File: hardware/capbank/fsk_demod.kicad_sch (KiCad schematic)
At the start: 14 parts, among them U10 TS861IL, U7 4046

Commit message: Small hardware changes
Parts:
- U7: value 4046 -> 74HC4046AD; footprint Package_DIP:DIP-16_W7.62mm -> Package_SO:SOIC-16_3.9x9.9mm_P1.27mm
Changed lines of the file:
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@@
 			)
 		)
-		(property "Value" "4046"
+		(property "Value" "74HC4046AD"
 			(at 69.4533 105.41 0)
 			(effects
@@
 			)
 		)
-		(property "Footprint" "Package_DIP:DIP-16_W7.62mm"
+		(property "Footprint" "Package_SO:SOIC-16_3.9x9.9mm_P1.27mm"
 			(at 67.31 120.65 0)
 			(effects

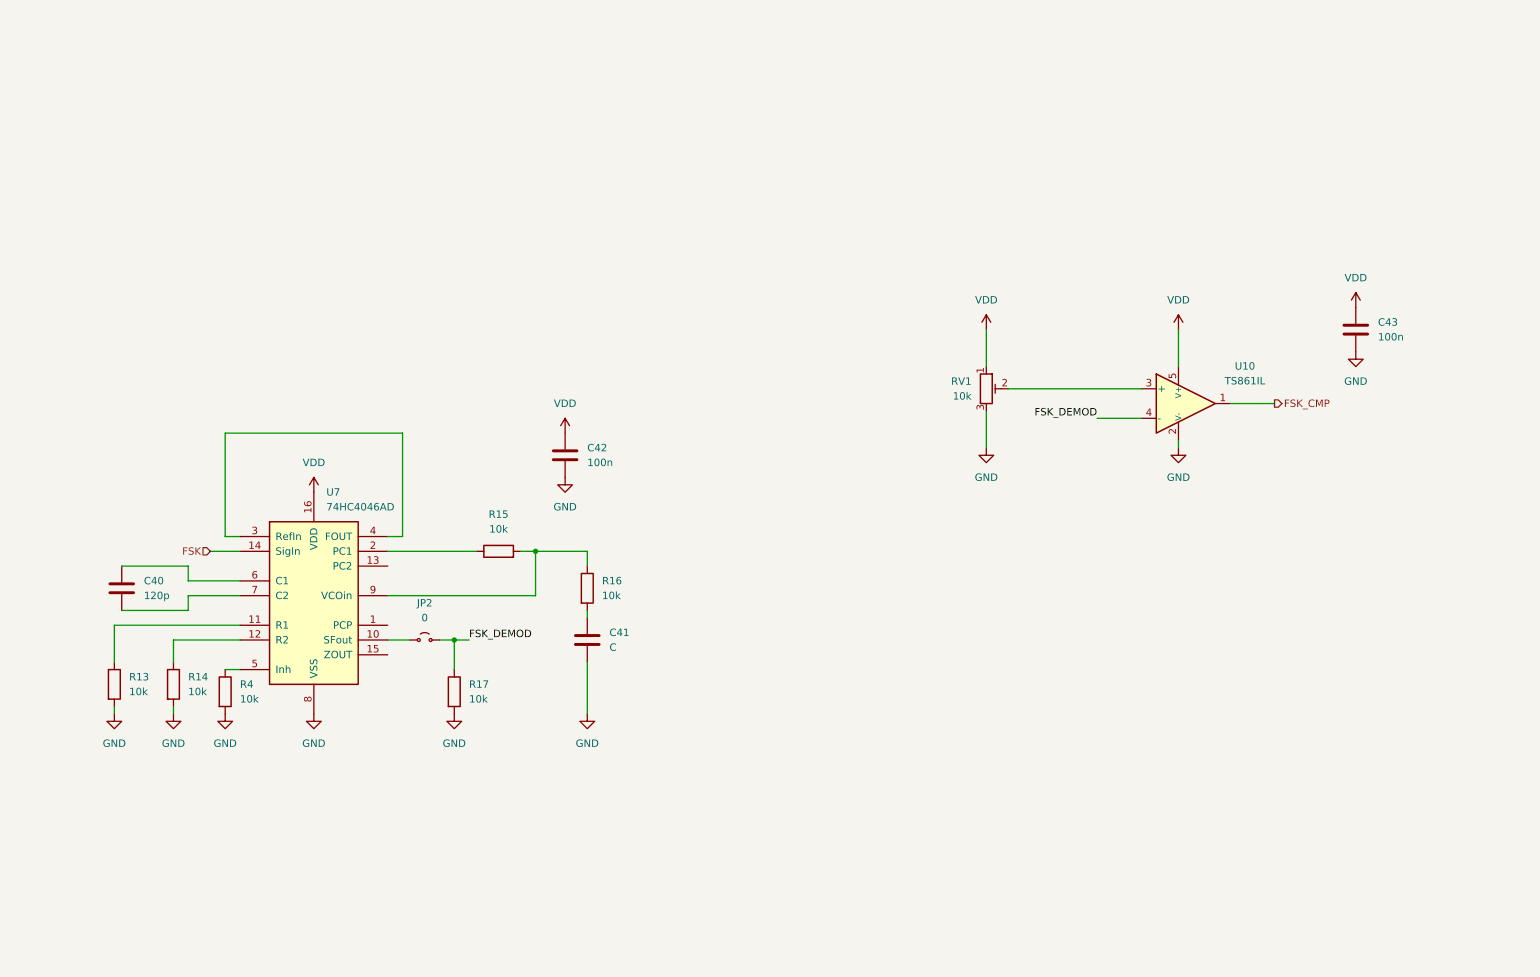
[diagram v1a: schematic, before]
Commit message: Add footprint for buffered-filter and replace pot with digital pot
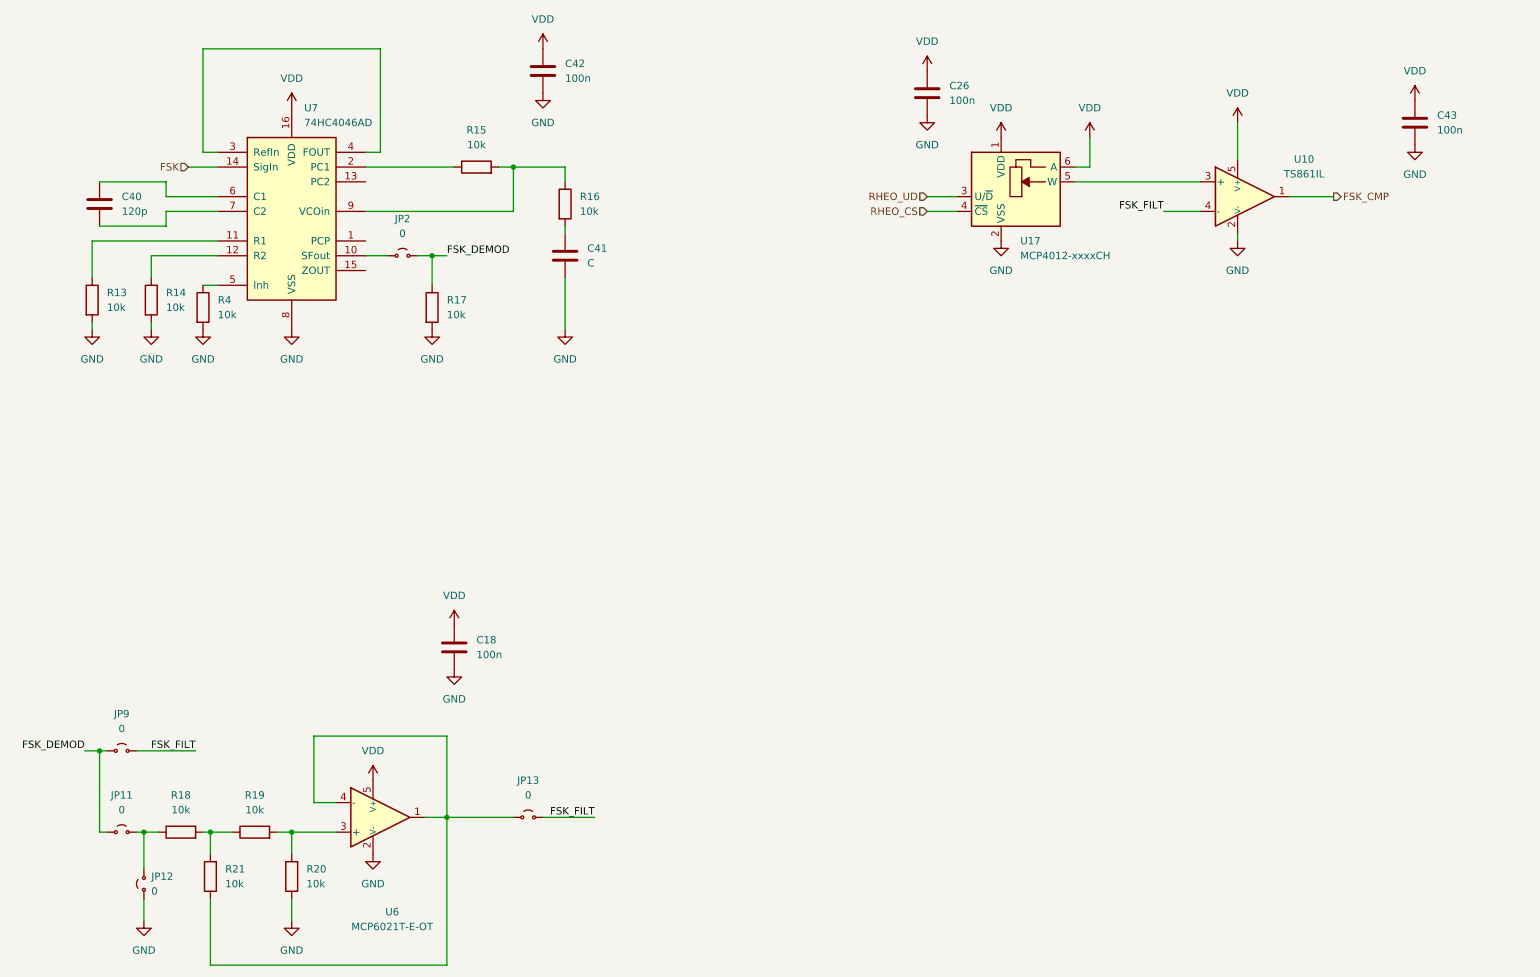
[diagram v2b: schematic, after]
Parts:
- removed RV1: 10k, PCM_Potentiometer_THT_AKL:Potentiometer_Piher_PT-10-V10_Vertical, symbol Device:R_Potentiometer_Trim
- added C18, C26: 100n, PCM_Capacitor_SMD_AKL:C_0603_1608Metric, symbol Device:C
- added JP11, JP12, JP13, JP9: 0, PCM_Resistor_SMD_AKL:R_0603_1608Metric, symbol Jumper:Jumper_2_Small_Open
- added R18, R19, R20, R21: 10k, PCM_Resistor_SMD_AKL:R_0603_1608Metric, symbol Device:R
- added U17: MCP4012-xxxxCH, Package_TO_SOT_SMD:SOT-23-6, symbol Potentiometer_Digital:MCP4012-xxxxCH
- added U6: MCP6021T-E-OT, PCM_Package_TO_SOT_SMD_AKL:SOT-23-5, symbol PCM_Amplifier_Operational_AKL:MCP6021T-E-OT
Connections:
- net FSK_DEMOD: now also JP11.1 (A), JP9.1 (A); no longer U10.4 (-)
- net GND: now also C18.2, C26.2, JP12.1 (A), R20.1, U17.2 (VSS), U6.2 (V-)
- net VDD: now also C18.1, C26.1, U17.1 (VDD), U17.6 (A), U6.5 (V+)
- net at U10.3 (+): now also U17.5 (W)
- new net: JP11.2 (B), JP12.2 (B), R18.1
- new net: R18.2, R19.1, R21.2
- new net: R19.2, R20.2, U6.3 (+)
- new net: JP13.1 (A), R21.1, U6.1, U6.4 (-)
- new net FSK_FILT: JP13.2 (B), JP9.2 (B), U10.4 (-)
- new net RHEO_CS: U17.4 (~{CS})
- new net RHEO_UD: U17.3 (U/~{D})
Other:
- moved on the sheet: C40, C41, C42, C43, JP2, R13, R14, R15, R16, R17, R4, U10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

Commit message: Update PCB with learned lessons
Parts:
- added C34: 100n, PCM_Capacitor_SMD_AKL:C_0603_1608Metric, symbol Device:C
- added JP14, JP15, JP16: 0, PCM_Resistor_SMD_AKL:R_0603_1608Metric, symbol Jumper:Jumper_2_Small_Open
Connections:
- net GND: now also C34.2
- net VCO_IN: now reaches R15.2, R16.1, U7.9 (VCOin)
- net VCO_IN: now also C34.1
- net at U7.2 (PC1): now also JP16.1 (A); no longer R15.1
- net at U7.13 (PC2): now also JP15.1 (A)
- net at U7.15 (ZOUT): now also JP14.1 (A)
- new net PC: JP14.2 (B), JP15.2 (B), JP16.2 (B), R15.1
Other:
- moved on the sheet: C26, C41, C43, JP2, R15, R16, R17, U10, U17

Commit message: Add hysteresis to comparator
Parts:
- removed R20, R21: 10k, PCM_Resistor_SMD_AKL:R_0603_1608Metric, symbol Device:R
- removed U17: MCP4012-xxxxCH, Package_TO_SOT_SMD:SOT-23-6, symbol Potentiometer_Digital:MCP4012-xxxxCH
- added C14, C36: 1n, PCM_Capacitor_SMD_AKL:C_0603_1608Metric, symbol Device:C
- added R25: 10k, PCM_Resistor_SMD_AKL:R_0603_1608Metric, symbol Device:R
- added R26: 200k, PCM_Resistor_SMD_AKL:R_0603_1608Metric, symbol Device:R
- added U18: MCP4013-xxxxCH, Package_TO_SOT_SMD:SOT-23-6, symbol Potentiometer_Digital:MCP4013-xxxxCH
- C34: value 100n -> 1n
- C41: value C -> 100n
- R15: value 10k -> 285k
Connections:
- net FSK_CMP: now also R26.1
- net GND: now also C14.2, U18.2 (VSS)
- net RHEO_CS: now also U18.4 (~{CS})
- net RHEO_UD: now also U18.3 (U/~{D})
- net VDD: now also U18.1 (VDD), U18.6 (A)
- net at U10.3 (+): now also R25.2, R26.2
- net at R18.2, R19.1: now also C36.1
- net at R19.2, U6.3 (+): now also C14.1
- net at JP13.1 (A), U6.1, U6.4 (-): now also C36.2
- new net: R25.1, U18.5 (W)
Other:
- note added: "For 74HC_HCT4046A (dataset names): fl = 100kHz R1C1 = 4e-5 (40us) foff = 90kHz R2 = 150kOhm C1 = 700pF R1 = 57kOhm (R2C1 = 105us)"
- note added: "For cd74hc4046a (dataset names): f0 = 250kHz fl = 100kHz fmin = 90kHz fmax = 410kHz VCC = 5V R2 = 22k C1 = 2~3nF R2/R1 = ~3 R1 = 7.4k (maybe a bit lower) (R1C1 = 18.5us) (R2C1 = 55us)"
- note added: "I[output positive] = (VCC - x * VCC) / (R26 + R_series) I[output negative] = x * VCC / (R26 + R_series)"
- note added: "Thevenin equivalent R_series = x (1-x) * 10k + R25 V = x * VCC"
- note added: "Up to first order, for R26 >> R25 and R_[MCP] ~= R25: V+[output positive] = VCC * x + VCC * R25 / R26 V+[output negative] = VCC * x - VCC * R25 / R26 V+[output positive] > V+[output_negative] (If FSK_FILT < V+, output is positive, once FSK_FILT crosses V+, output jumps to negative, and as expected the V+ jumps a bit downwards)"
- moved on the sheet: C34, C41, R15, R16

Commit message: Various wiring fixes and add bleed resistor to antenna
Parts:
- C36: value 1n -> 2n
- R18, R19: value 10k -> 1.7k
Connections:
- no-connect marks 0 -> 1
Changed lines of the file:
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@@
 		(color 0 0 0 0)
 	)
+	(no_connect
+		(at 76.2 59.69)
+	)
 	(wire
 		(pts
@@
 			)
 		)
-		(property "Value" "10k"
+		(property "Value" "1.7k"
 			(at 44.45 157.48 90)
 			(effects
@@
 			)
 		)
-		(property "Value" "10k"
+		(property "Value" "1.7k"
 			(at 57.15 157.48 90)
 			(effects
@@
 			)
 		)
-		(property "Value" "1n"
+		(property "Value" "2n"
 			(at 53.34 170.1799 0)
 			(effects

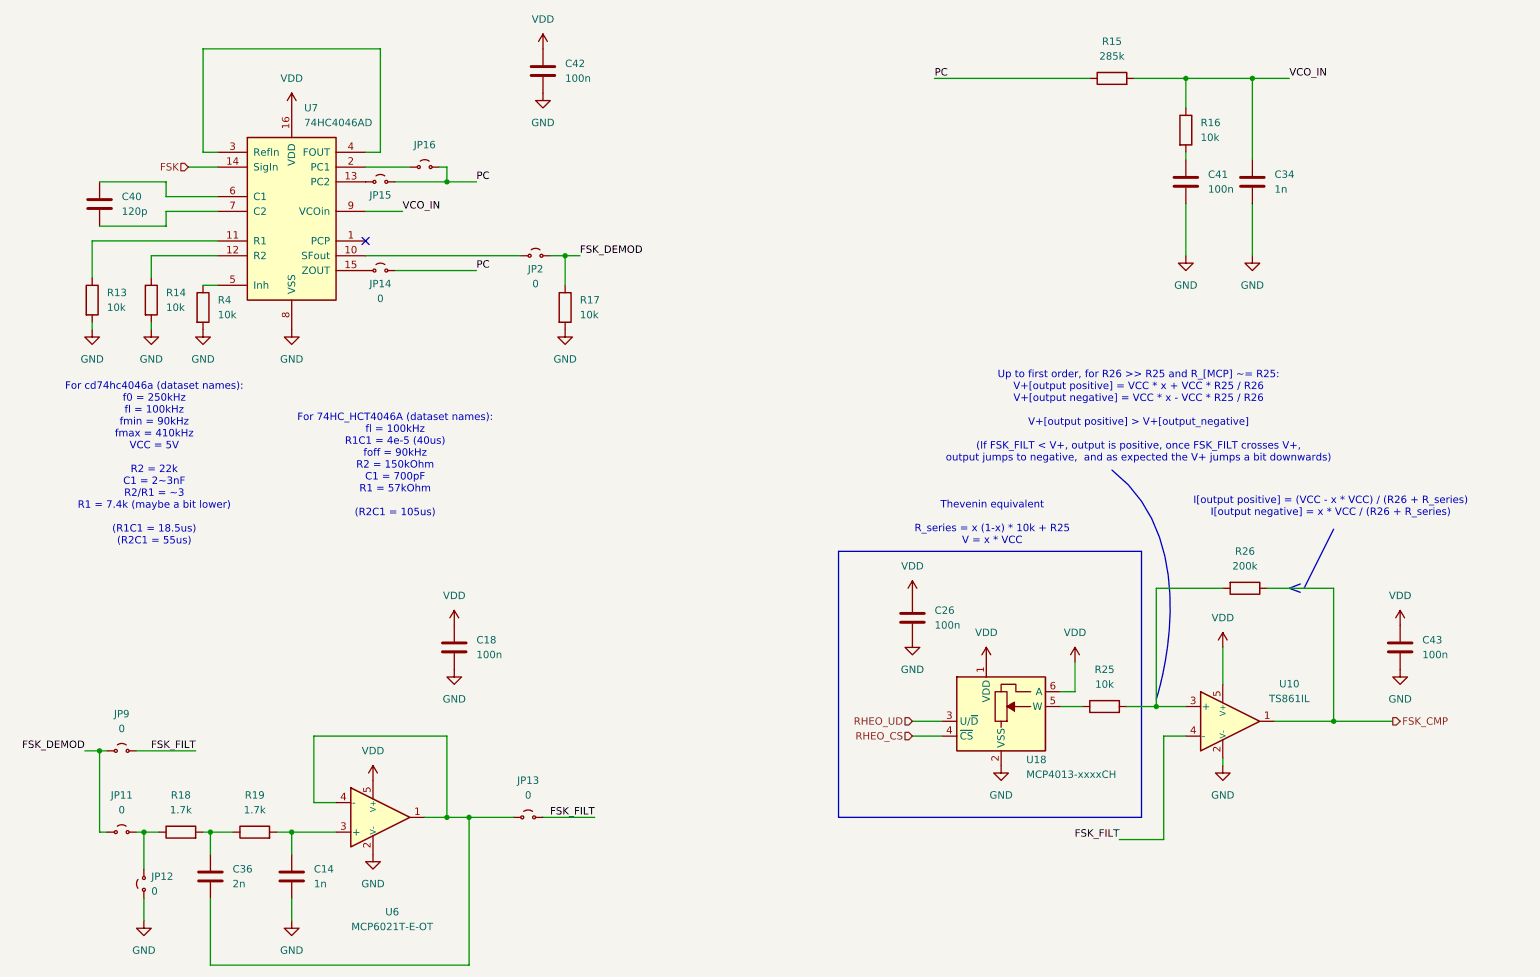
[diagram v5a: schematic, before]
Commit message: Update values after breadboard testing
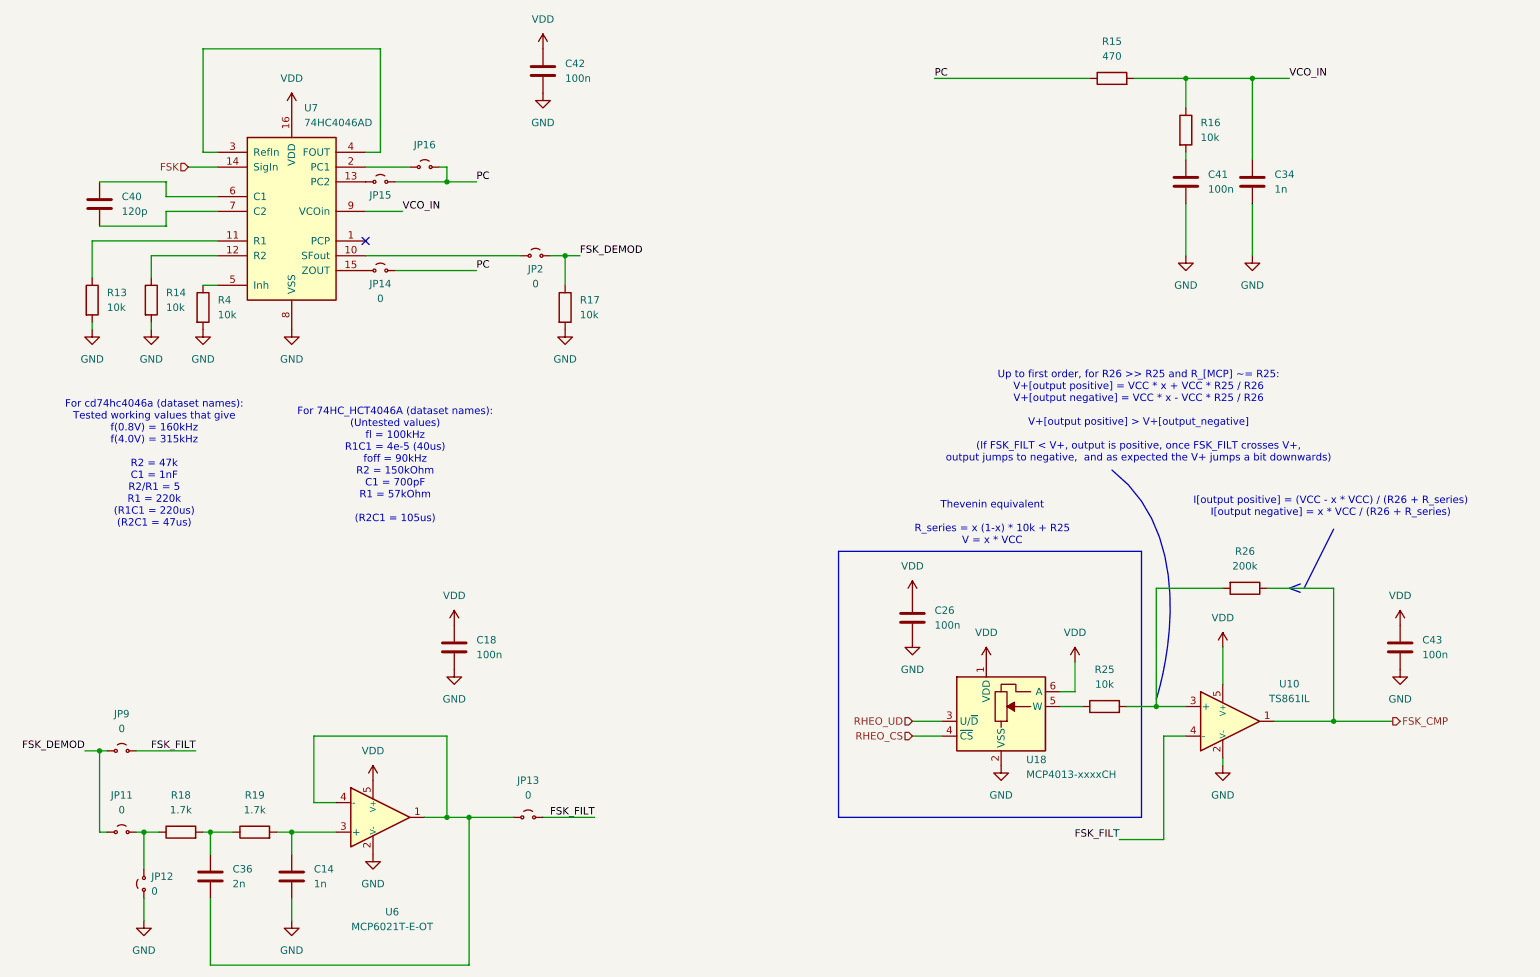
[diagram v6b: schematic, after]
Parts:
- R15: value 285k -> 470
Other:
- note added: "For 74HC_HCT4046A (dataset names): (Untested values) fl = 100kHz R1C1 = 4e-5 (40us) foff = 90kHz R2 = 150kOhm C1 = 700pF R1 = 57kOhm (R2C1 = 105us)"
- note added: "For cd74hc4046a (dataset names): Tested working values that give f(0.8V) = 160kHz f(4.0V) = 315kHz R2 = 47k C1 = 1nF R2/R1 = 5 R1 = 220k (R1C1 = 220us) (R2C1 = 47us)"
- note removed: "For 74HC_HCT4046A (dataset names): fl = 100kHz R1C1 = 4e-5 (40us) foff = 90kHz R2 = 150kOhm C1 = 700pF R1 = 57kOhm (R2C1 = 105us)"
- note removed: "For cd74hc4046a (dataset names): f0 = 250kHz fl = 100kHz fmin = 90kHz fmax = 410kHz VCC = 5V R2 = 22k C1 = 2~3nF R2/R1 = ~3 R1 = 7.4k (maybe a bit lower) (R1C1 = 18.5us) (R2C1 = 55us)"
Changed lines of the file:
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@@
 		)
 	)
-	(text "For cd74hc4046a (dataset names):\nf0 = 250kHz\nfl = 100kHz\nfmin = 90kHz \nfmax = 410kHz\nVCC = 5V\n\nR2 = 22k\nC1 = 2~3nF\nR2/R1 = ~3\nR1 = 7.4k (maybe a bit lower)\n\n(R1C1 = 18.5us)\n(R2C1 = 55us)"
+	(text "For cd74hc4046a (dataset names):\nTested working values that give \nf(0.8V) = 160kHz\nf(4.0V) = 315kHz\n\nR2 = 47k\nC1 = 1nF\nR2/R1 = 5\nR1 = 220k\n(R1C1 = 220us)\n(R2C1 = 47us)"
 		(exclude_from_sim no)
 		(at 39.878 98.044 0)
@@
 		)
 	)
-	(text "For 74HC_HCT4046A (dataset names):\nfl = 100kHz\nR1C1 = 4e-5 (40us)\nfoff = 90kHz\nR2 = 150kOhm\nC1 = 700pF\nR1 = 57kOhm\n\n(R2C1 = 105us)"
+	(text "For 74HC_HCT4046A (dataset names):\n(Untested values)\nfl = 100kHz\nR1C1 = 4e-5 (40us)\nfoff = 90kHz\nR2 = 150kOhm\nC1 = 700pF\nR1 = 57kOhm\n\n(R2C1 = 105us)"
 		(exclude_from_sim no)
 		(at 81.28 98.298 0)
@@
 			)
 		)
-		(property "Value" "285k"
+		(property "Value" "470"
 			(at 204.47 27.94 90)
 			(effects
@@
 		)
 		(instances
-			(project ""
+			(project "capbank1"
 				(path "/461cb8a1-2d60-44a8-88b5-d61a3ba14a84/d9c36704-5831-4033-b353-abc8255d1c86/9a2777cd-eff3-4d8b-a149-a95a84199cc5"
 					(reference "U18")
@@
 		)
 		(instances
-			(project ""
+			(project "capbank1"
 				(path "/461cb8a1-2d60-44a8-88b5-d61a3ba14a84/d9c36704-5831-4033-b353-abc8255d1c86/9a2777cd-eff3-4d8b-a149-a95a84199cc5"
 					(reference "U6")
